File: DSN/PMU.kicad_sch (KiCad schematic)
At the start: 58 parts

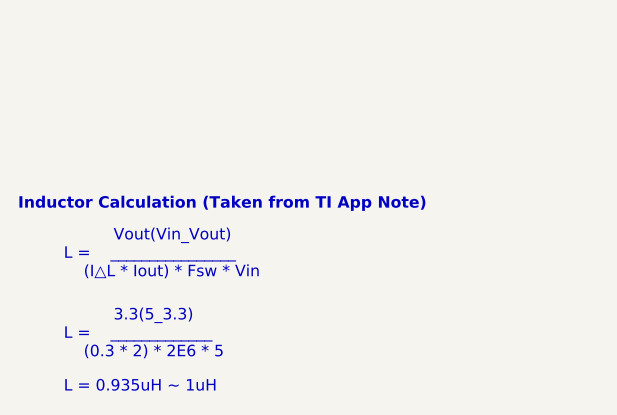
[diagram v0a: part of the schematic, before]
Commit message: Updates
Changed FPGA user io from 100 to 50 per chip, added 4 pmod per FPGA, added 8x buttons + led's, added SMA connectors for FPGA0 GTP.
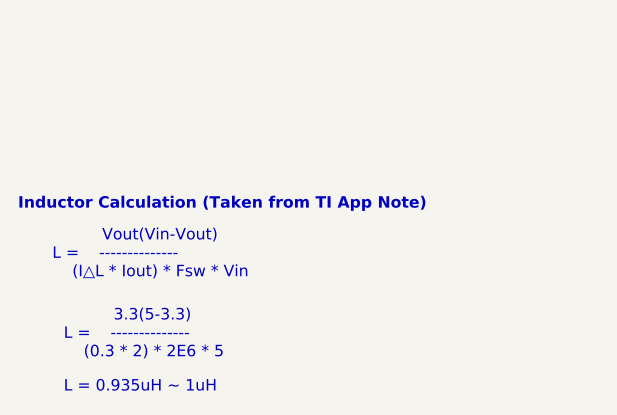
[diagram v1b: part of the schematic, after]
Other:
- note added: "3.3(5-3.3) L = -------------- (0.3 * 2) * 2E6 * 5"
- note added: "Vout(Vin-Vout) L = -------------- (I△L * Iout) * Fsw * Vin"
- note removed: "3.3(5_3.3) L = _____________ (0.3 * 2) * 2E6 * 5"
- note removed: "Vout(Vin_Vout) L = ________________ (I△L * Iout) * Fsw * Vin"
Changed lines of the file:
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@@
     (effects (font (size 1.27 1.27) bold) (justify left bottom))
   )
-  (text "      	Vout(Vin_Vout)\nL =	________________\n	(I△L * Iout) * Fsw * Vin"
-    (at 20.32 262.89 0)
+  (text "      	Vout(Vin-Vout)\nL =	--------------\n	(I△L * Iout) * Fsw * Vin"
+    (at 19.05 262.89 0)
     (effects (font (size 1.27 1.27)) (justify left bottom))
   )
@@
     (effects (font (size 1.27 1.27)) (justify left bottom))
   )
-  (text "      	3.3(5_3.3)\nL =	_____________\n	(0.3 * 2) * 2E6 * 5"
+  (text "      	3.3(5-3.3)\nL =	--------------\n	(0.3 * 2) * 2E6 * 5"
     (at 20.32 271.78 0)
     (effects (font (size 1.27 1.27)) (justify left bottom))

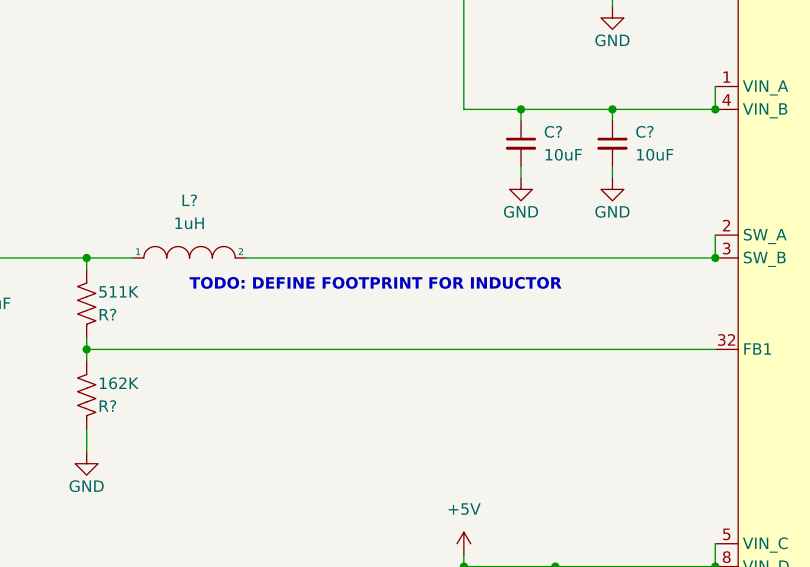
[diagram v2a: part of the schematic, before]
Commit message: Added Footprints
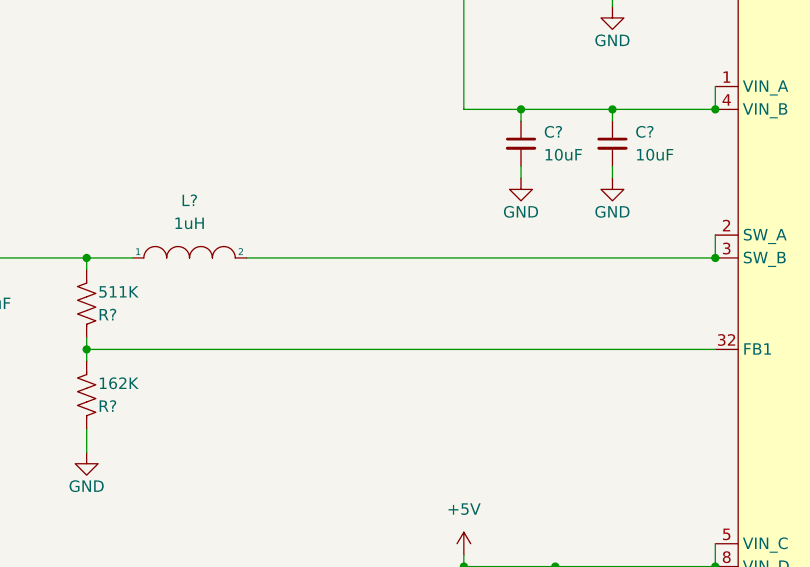
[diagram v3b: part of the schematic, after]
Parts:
- removed L? (x3): 1uH, Inductor_SMD:L_Coilcraft_XxL4040, symbol pspice:INDUCTOR
- added L? (x3): 1uH, Inductor_SMD:L_Coilcraft_XxL4020, symbol pspice:INDUCTOR
- L?: footprint Inductor_SMD:L_Coilcraft_XxL4040 -> Inductor_SMD:L_Coilcraft_XxL4020
- U?: footprint (none) -> Package_DFN_QFN:QFN-32-1EP_5x5mm_P0.5mm_EP3.45x3.45mm_ThermalVias; MFR PN (none) -> LTC3370IUH#PBF
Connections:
- net at C?.1, C?.1, C?.1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: now also L?.1
- net at C?.1, C?.1, C?.1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: now also L?.2 (x2)
- net at U?.22 (SW_G), U?.23 (SW_H): now also L?.1
- net at U?.6 (SW_C), U?.7 (SW_D): now also L?.2
- net at U?.18 (SW_E), U?.19 (SW_F): now also L?.1
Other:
- note removed: "TODO: DEFINE FOOTPRINT FOR INDUCTOR"
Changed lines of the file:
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@@
     (effects (font (size 1.27 1.27)) (justify left bottom))
-  )
-  (text "TODO: DEFINE FOOTPRINT FOR INDUCTOR" (at 146.05 106.68 0)
-    (effects (font (size 1.27 1.27) bold) (justify left bottom))
   )
   (text "All channeles disabled by default with pulldowns\n" (at 142.24 222.25 0)
@@
     )
     (property "MFR PN" "RC0402FR-07162KL" (id 4) (at 302.26 158.75 0)
-      (effects (font (size 1.27 1.27)) hide)
-    )
-    (pin "1")
-    (pin "2")
-  )
-  (symbol (lib_id "pspice:INDUCTOR") (at 281.94 153.67 0) (unit 1)
-    (in_bom yes) (on_board yes) (fields_autoplaced)
-    (property "Reference" "L?" (id 0) (at 281.94 147.32 0))
-    (property "Value" "1uH" (id 1) (at 281.94 149.86 0))
-    (property "Footprint" "Inductor_SMD:L_Coilcraft_XxL4040" (id 2) (at 281.94 153.67 0)
-      (effects (font (size 1.27 1.27)) hide)
-    )
-    (property "Datasheet" "https://www.mouser.com/datasheet/2/597/xfl4020-270756.pdf" (id 3) (at 281.94 153.67 0)
-      (effects (font (size 1.27 1.27)) hide)
-    )
-    (property "MFR PN" "XFL4020-102MEC " (id 4) (at 281.94 153.67 0)
       (effects (font (size 1.27 1.27)) hide)
     )
@@
     (pin "9")
   )
-  (symbol (lib_id "pspice:INDUCTOR") (at 146.05 153.67 0) (unit 1)
-    (in_bom yes) (on_board yes) (fields_autoplaced)
-    (property "Reference" "L?" (id 0) (at 146.05 147.32 0))
-    (property "Value" "1uH" (id 1) (at 146.05 149.86 0))
-    (property "Footprint" "Inductor_SMD:L_Coilcraft_XxL4040" (id 2) (at 146.05 153.67 0)
-      (effects (font (size 1.27 1.27)) hide)
-    )
-    (property "Datasheet" "https://www.mouser.com/datasheet/2/597/xfl4020-270756.pdf" (id 3) (at 146.05 153.67 0)
-      (effects (font (size 1.27 1.27)) hide)
-    )
-    (property "MFR PN" "XFL4020-102MEC " (id 4) (at 146.05 153.67 0)
-      (effects (font (size 1.27 1.27)) hide)
-    )
-    (pin "1")
-    (pin "2")
-  )
   (symbol (lib_id "Device:R_US") (at 270.51 200.66 90) (unit 1)
     (in_bom yes) (on_board yes)
@@
     (property "Reference" "L?" (id 0) (at 146.05 96.52 0))
     (property "Value" "1uH" (id 1) (at 146.05 99.06 0))
-    (property "Footprint" "Inductor_SMD:L_Coilcraft_XxL4040" (id 2) (at 146.05 102.87 0)
+    (property "Footprint" "Inductor_SMD:L_Coilcraft_XxL4020" (id 2) (at 146.05 102.87 0)
       (effects (font (size 1.27 1.27)) hide)
     )
@@
     (pin "1")
   )
+  (symbol (lib_id "pspice:INDUCTOR") (at 281.94 153.67 0) (unit 1)
+    (in_bom yes) (on_board yes) (fields_autoplaced)
+    (property "Reference" "L?" (id 0) (at 281.94 147.32 0))
+    (property "Value" "1uH" (id 1) (at 281.94 149.86 0))
+    (property "Footprint" "Inductor_SMD:L_Coilcraft_XxL4020" (id 2) (at 281.94 153.67 0)
+      (effects (font (size 1.27 1.27)) hide)
+    )
+    (property "Datasheet" "https://www.mouser.com/datasheet/2/597/xfl4020-270756.pdf" (id 3) (at 281.94 153.67 0)
+      (effects (font (size 1.27 1.27)) hide)
+    )
+    (property "MFR PN" "XFL4020-102MEC " (id 4) (at 281.94 153.67 0)
+      (effects (font (size 1.27 1.27)) hide)
+    )
+    (pin "1")
+    (pin "2")
+  )
   (symbol (lib_id "power:+5V") (at 276.86 217.17 0) (unit 1)
     (in_bom yes) (on_board yes) (fields_autoplaced)
@@
     (property "Reference" "U?" (id 0) (at 218.44 60.96 0))
     (property "Value" "LTC3370" (id 1) (at 218.44 63.5 0))
-    (property "Footprint" "" (id 2) (at 207.01 147.32 0)
-      (effects (font (size 1.27 1.27)) hide)
-    )
-    (property "Datasheet" "" (id 3) (at 207.01 147.32 0)
+    (property "Footprint" "Package_DFN_QFN:QFN-32-1EP_5x5mm_P0.5mm_EP3.45x3.45mm_ThermalVias" (id 2) (at 207.01 147.32 0)
+      (effects (font (size 1.27 1.27)) hide)
+    )
+    (property "Datasheet" "https://www.analog.com/media/en/technical-documentation/data-sheets/3370fb.pdf" (id 3) (at 207.01 147.32 0)
+      (effects (font (size 1.27 1.27)) hide)
+    )
+    (property "MFR PN" "LTC3370IUH#PBF" (id 4) (at 207.01 147.32 0)
       (effects (font (size 1.27 1.27)) hide)
     )
@@
       (effects (font (size 1.27 1.27)) hide)
     )
-    (property "Datasheet" "~" (id 3) (at 220.98 38.1 0)
+    (property "Datasheet" "https://www.mouser.com/datasheet/2/447/PYu_RC_Group_51_RoHS_L_11-1984063.pdf" (id 3) (at 220.98 38.1 0)
       (effects (font (size 1.27 1.27)) hide)
     )
     (property "MRF PN" "RC0402FR-070RL" (id 4) (at 220.98 38.1 90)
-      (effects (font (size 1.27 1.27)) hide)
-    )
-    (pin "1")
-    (pin "2")
-  )
-  (symbol (lib_id "Device:C_Small") (at 119.38 106.68 0) (unit 1)
-    (in_bom yes) (on_board yes) (fields_autoplaced)
-    (property "Reference" "C?" (id 0) (at 121.92 105.4162 0)
-      (effects (font (size 1.27 1.27)) (justify left))
-    )
-    (property "Value" "22uF" (id 1) (at 121.92 107.9562 0)
-      (effects (font (size 1.27 1.27)) (justify left))
-    )
-    (property "Footprint" "Capacitor_SMD:C_1206_3216Metric" (id 2) (at 119.38 106.68 0)
-      (effects (font (size 1.27 1.27)) hide)
-    )
-    (property "Datasheet" "https://www.mouser.com/datasheet/2/281/GCM31CR71A226KE02_01-1969540.pdf" (id 3) (at 119.38 106.68 0)
-      (effects (font (size 1.27 1.27)) hide)
-    )
-    (property "MFR PN" "GCM31CR71A226KE02L" (id 4) (at 119.38 106.68 0)
       (effects (font (size 1.27 1.27)) hide)
     )
@@
     (property "Reference" "L?" (id 0) (at 281.94 96.52 0))
     (property "Value" "1uH" (id 1) (at 281.94 99.06 0))
-    (property "Footprint" "Inductor_SMD:L_Coilcraft_XxL4040" (id 2) (at 281.94 102.87 0)
+    (property "Footprint" "Inductor_SMD:L_Coilcraft_XxL4020" (id 2) (at 281.94 102.87 0)
       (effects (font (size 1.27 1.27)) hide)
     )
@@
       (effects (font (size 1.27 1.27)) hide)
     )
+    (pin "1")
+    (pin "2")
+  )
+  (symbol (lib_id "Device:C_Small") (at 119.38 106.68 0) (unit 1)
+    (in_bom yes) (on_board yes) (fields_autoplaced)
+    (property "Reference" "C?" (id 0) (at 121.92 105.4162 0)
+      (effects (font (size 1.27 1.27)) (justify left))
+    )
+    (property "Value" "22uF" (id 1) (at 121.92 107.9562 0)
+      (effects (font (size 1.27 1.27)) (justify left))
+    )
+    (property "Footprint" "Capacitor_SMD:C_1206_3216Metric" (id 2) (at 119.38 106.68 0)
+      (effects (font (size 1.27 1.27)) hide)
+    )
+    (property "Datasheet" "https://www.mouser.com/datasheet/2/281/GCM31CR71A226KE02_01-1969540.pdf" (id 3) (at 119.38 106.68 0)
+      (effects (font (size 1.27 1.27)) hide)
+    )
+    (property "MFR PN" "GCM31CR71A226KE02L" (id 4) (at 119.38 106.68 0)
+      (effects (font (size 1.27 1.27)) hide)
+    )
+    (pin "1")
+    (pin "2")
+  )
+  (symbol (lib_id "pspice:INDUCTOR") (at 146.05 153.67 0) (unit 1)
+    (in_bom yes) (on_board yes) (fields_autoplaced)
+    (property "Reference" "L?" (id 0) (at 146.05 147.32 0))
+    (property "Value" "1uH" (id 1) (at 146.05 149.86 0))
+    (property "Footprint" "Inductor_SMD:L_Coilcraft_XxL4020" (id 2) (at 146.05 153.67 0)
+      (effects (font (size 1.27 1.27)) hide)
+    )
+    (property "Datasheet" "https://www.mouser.com/datasheet/2/597/xfl4020-270756.pdf" (id 3) (at 146.05 153.67 0)
+      (effects (font (size 1.27 1.27)) hide)
+    )
+    (property "MFR PN" "XFL4020-102MEC " (id 4) (at 146.05 153.67 0)
+      (effects (font (size 1.27 1.27)) hide)
+    )

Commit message: Added component ref des
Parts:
- gave numbers to parts that had none: 58

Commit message: Fixed all ERC Errors
Warnings can be ignored
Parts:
- added TP10, TP5, TP6, TP7, TP8, TP9: TestPoint_Probe, TestPoint:TestPoint_Loop_D2.50mm_Drill1.85mm, symbol Connector:TestPoint_Probe
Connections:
- net +3V3_ISNS: now also TP8.1
- net +5V: now also TP7.1
- net at C34.1, C36.1, C38.1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: now also TP5.1
- net at C52.1, C54.1, C56.1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: now also TP10.1
- net at C35.1, C37.1, C39.1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: now also TP6.1
- net at C51.1, C53.1, C55.1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: now also TP9.1
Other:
- moved on the sheet: R29, R30

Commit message: Initial PCB Layout
Initial layout and part placement
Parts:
- R41, R44: footprint (none) -> Resistor_SMD:R_0402_1005Metric
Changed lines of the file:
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@@
     (property "Reference" "R41" (id 0) (at 270.51 195.58 90))
     (property "Value" "NOSTUFF" (id 1) (at 270.51 198.12 90))
-    (property "Footprint" "" (id 2) (at 270.764 199.644 90)
+    (property "Footprint" "Resistor_SMD:R_0402_1005Metric" (id 2) (at 270.764 199.644 90)
       (effects (font (size 1.27 1.27)) hide)
     )
@@
     (property "Reference" "R44" (id 0) (at 270.51 223.52 90))
     (property "Value" "NOSTUFF" (id 1) (at 270.51 226.06 90))
-    (property "Footprint" "" (id 2) (at 270.764 219.964 90)
-      (effects (font (size 1.27 1.27)) hide)
-    )
+    (property "Footprint" "Resistor_SMD:R_0402_1005Metric" (id 2) (at 270.764 219.964 90)
+      (effects (font (size 1.27 1.27)) hide)
+    )

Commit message: Updated Layout
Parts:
- removed C38, C39, C40, C41, C51, C52, C53, C54: 22uF, Capacitor_SMD:C_1206_3216Metric, symbol Device:C_Small
- TP10, TP5, TP6, TP7, TP8, TP9: footprint TestPoint:TestPoint_Loop_D2.50mm_Drill1.85mm -> TestPoint:TestPoint_Loop_D1.80mm_Drill1.0mm_Beaded
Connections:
- net +1V0: now also U8.1 (IN+), U8.12 (VBUS), U8.2 (IN+), U8.3 (IN+); no longer U8.14 (IN-), U8.15 (IN-), U8.16 (IN-)
- net +1V8: now also U5.1 (IN+), U5.12 (VBUS), U5.2 (IN+), U5.3 (IN+); no longer U5.14 (IN-), U5.15 (IN-), U5.16 (IN-)
- net at C34.1, C36.1, L2.1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: now also U5.14 (IN-), U5.15 (IN-), U5.16 (IN-); no longer U5.1 (IN+), U5.12 (VBUS), U5.2 (IN+), U5.3 (IN+)
- net at C56.1, C58.1, L4.2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: now also U8.14 (IN-), U8.15 (IN-), U8.16 (IN-); no longer U8.1 (IN+), U8.12 (VBUS), U8.2 (IN+), U8.3 (IN+)
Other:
- moved on the sheet: C33, C60, U5, U8
